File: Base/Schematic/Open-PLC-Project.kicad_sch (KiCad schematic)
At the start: 0 parts

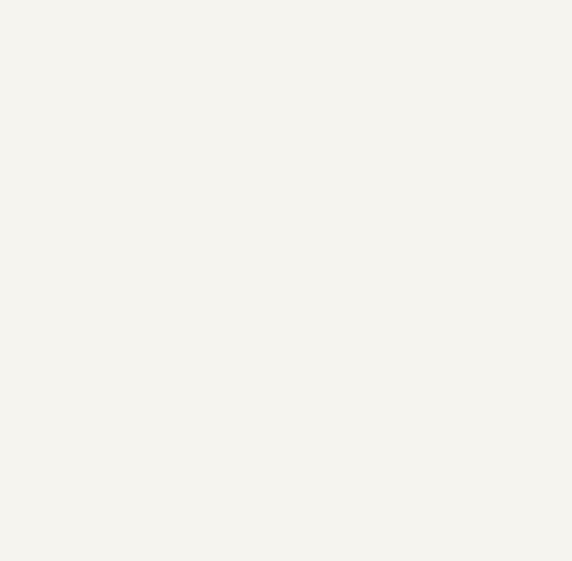
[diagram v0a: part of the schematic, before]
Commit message: [Base 회로 업데이트] - 전원 회로 추가
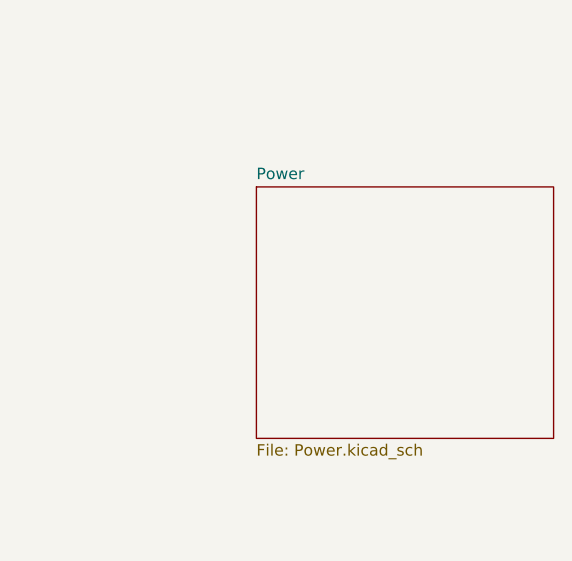
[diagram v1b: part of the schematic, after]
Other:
- added sheet Power (Power.kicad_sch)
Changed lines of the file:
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@@
+		)
+	)
+	(sheet
+		(at 223.52 127)
+		(size 33.02 27.94)
+		(fields_autoplaced yes)
+		(stroke
+			(width 0.1524)
+			(type solid)
+		)
+		(fill
+			(color 0 0 0 0.0000)
+		)
+		(property "Sheetname" "Power"
+			(at 223.52 126.2884 0)
+			(effects
+				(font
+					(size 1.27 1.27)
+				)
+				(justify left bottom)
+			)
+		)
+		(property "Sheetfile" "Power.kicad_sch"
+			(at 223.52 155.5246 0)
+			(effects
+				(font
+					(size 1.27 1.27)
+				)
+				(justify left top)
+			)
+		)
+		(instances
+			(project "Open-PLC-Project"
+				(path "/0d177ca6-e392-45a0-9514-d370436392ef"
+					(page "3")
+				)
+			)
 		)
 	)

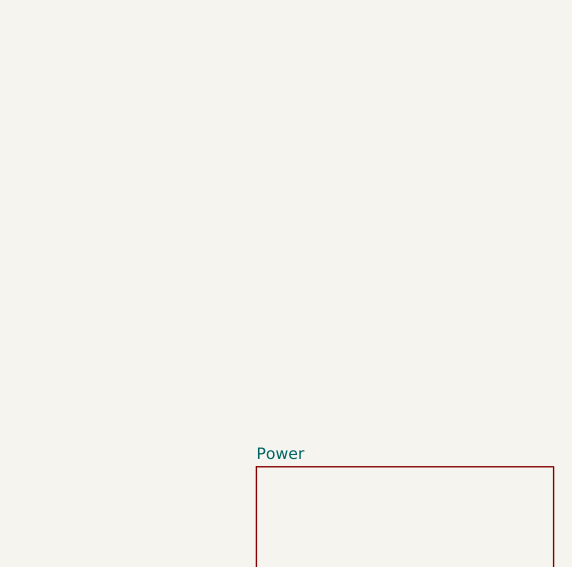
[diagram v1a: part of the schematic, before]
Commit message: [BOM 문서 테스트] - Libreoffice로 BOM 문서 출력 테스트 - 회로도에 CAN transceiver 추가
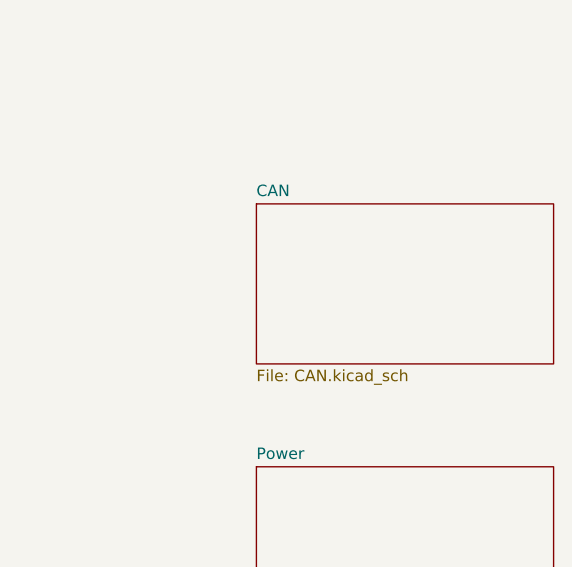
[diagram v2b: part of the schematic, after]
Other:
- added sheet CAN (CAN.kicad_sch)
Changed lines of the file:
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@@
+		)
+	)
+	(sheet
+		(at 223.52 97.79)
+		(size 33.02 17.78)
+		(fields_autoplaced yes)
+		(stroke
+			(width 0.1524)
+			(type solid)
+		)
+		(fill
+			(color 0 0 0 0.0000)
+		)
+		(property "Sheetname" "CAN"
+			(at 223.52 97.0784 0)
+			(effects
+				(font
+					(size 1.27 1.27)
+				)
+				(justify left bottom)
+			)
+		)
+		(property "Sheetfile" "CAN.kicad_sch"
+			(at 223.52 116.1546 0)
+			(effects
+				(font
+					(size 1.27 1.27)
+				)
+				(justify left top)
+			)
+		)
+		(instances
+			(project "Open-PLC-Project"
+				(path "/0d177ca6-e392-45a0-9514-d370436392ef"
+					(page "4")
+				)
+			)
 		)
 	)

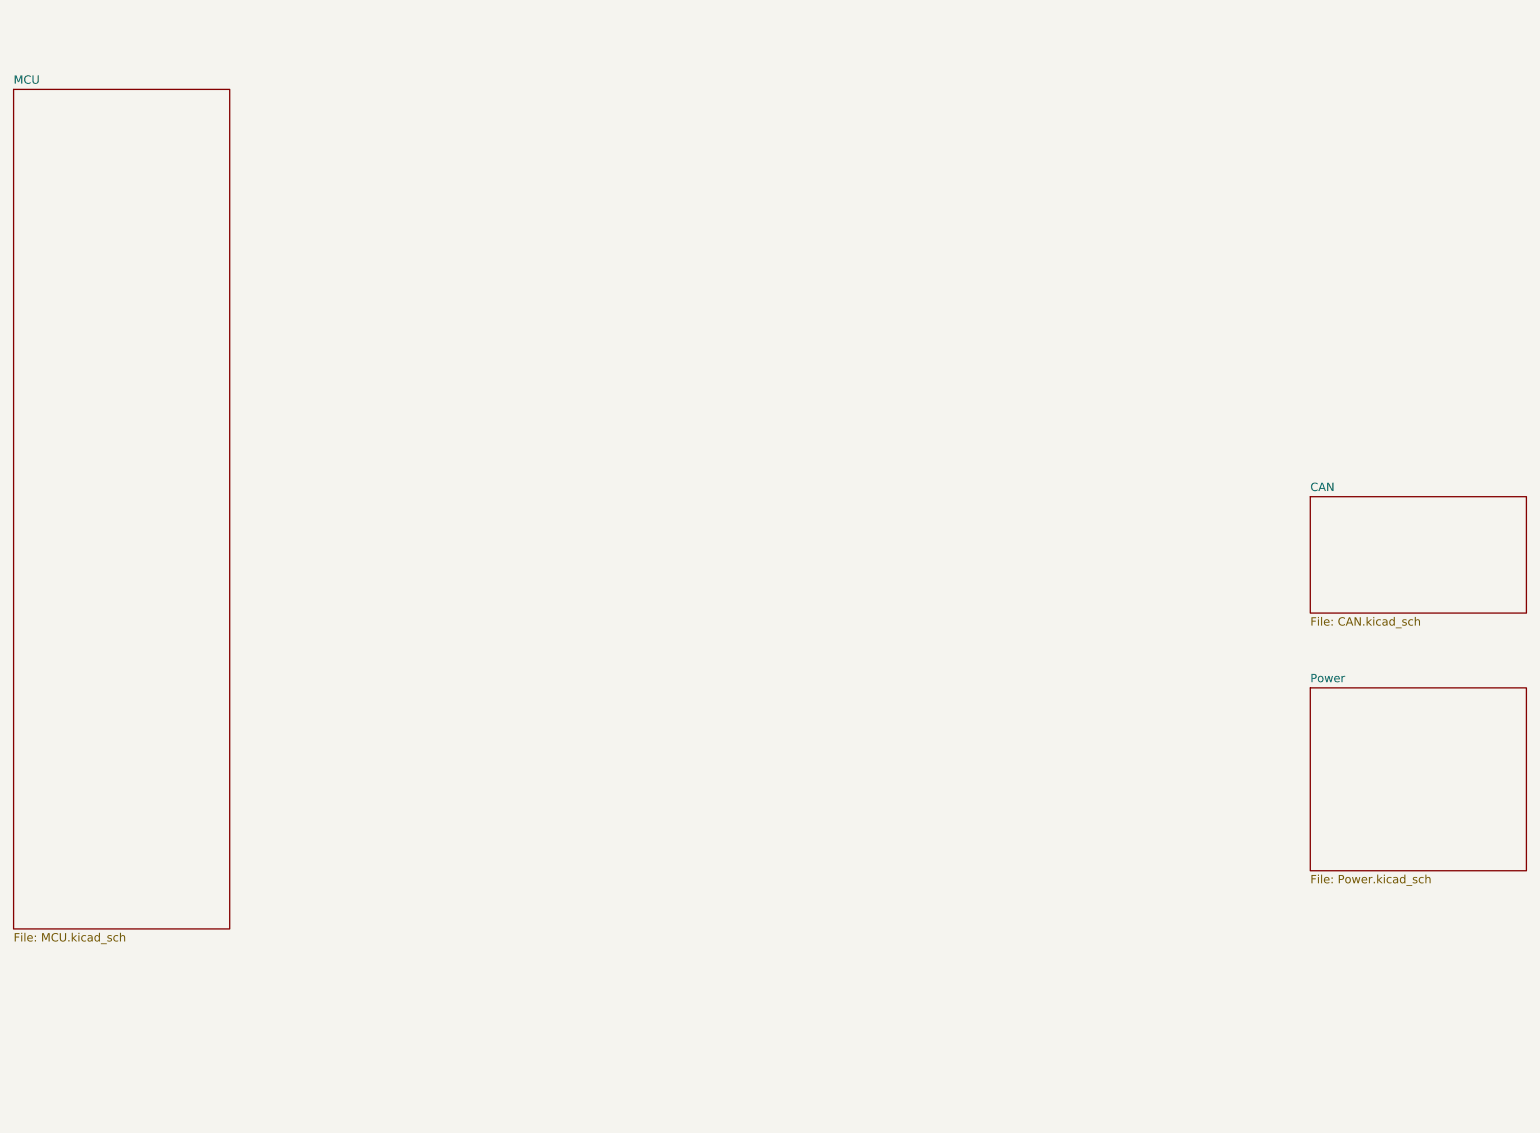
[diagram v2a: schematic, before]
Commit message: [Base 회로도 업데이트] - RS485 회로 추가
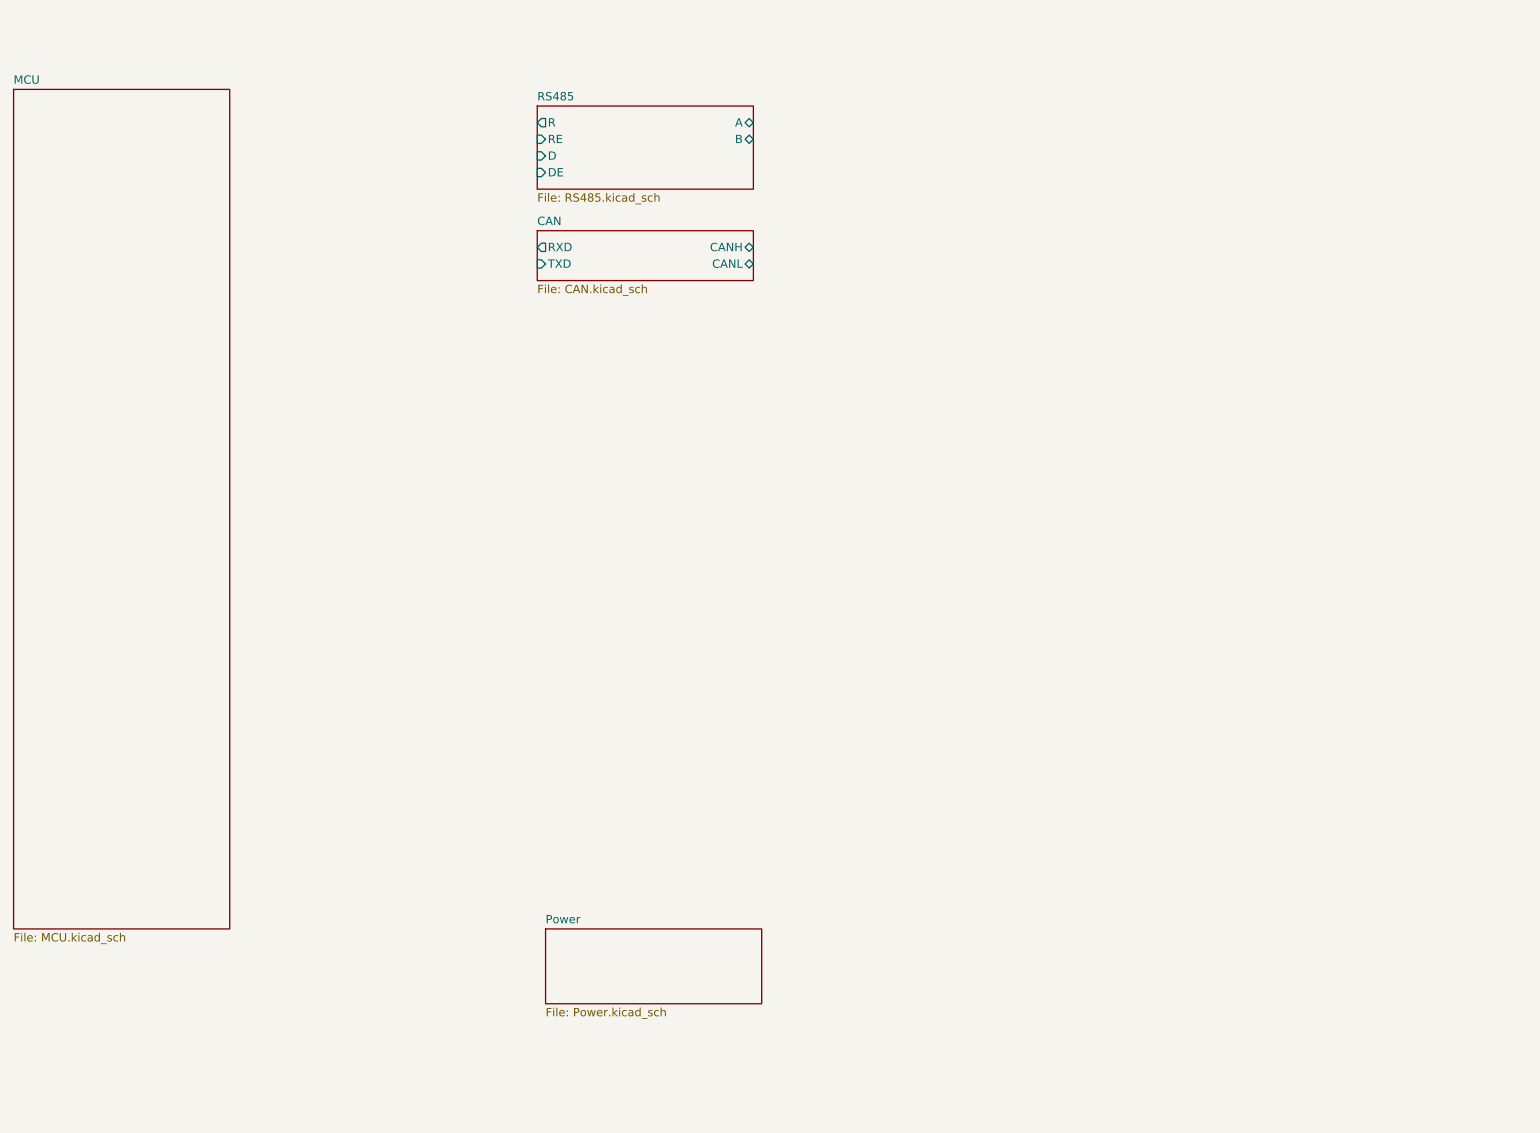
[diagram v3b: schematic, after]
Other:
- added sheet RS485 (RS485.kicad_sch)
- sheet CAN ports: added CANH, CANL, RXD, TXD; removed none
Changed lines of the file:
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@@
 	)
 	(sheet
-		(at 223.52 127)
-		(size 33.02 27.94)
+		(at 106.68 163.83)
+		(size 33.02 11.43)
 		(fields_autoplaced yes)
 		(stroke
@@
 		)
 		(property "Sheetname" "Power"
-			(at 223.52 126.2884 0)
+			(at 106.68 163.1184 0)
 			(effects
 				(font
@@
 		)
 		(property "Sheetfile" "Power.kicad_sch"
-			(at 223.52 155.5246 0)
+			(at 106.68 175.8446 0)
 			(effects
 				(font
@@
 	)
 	(sheet
-		(at 223.52 97.79)
-		(size 33.02 17.78)
+		(at 105.41 38.1)
+		(size 33.02 12.7)
+		(fields_autoplaced yes)
+		(stroke
+			(width 0.1524)
+			(type solid)
+		)
+		(fill
+			(color 0 0 0 0.0000)
+		)
+		(property "Sheetname" "RS485"
+			(at 105.41 37.3884 0)
+			(effects
+				(font
+					(size 1.27 1.27)
+				)
+				(justify left bottom)
+			)
+		)
+		(property "Sheetfile" "RS485.kicad_sch"
+			(at 105.41 51.3846 0)
+			(effects
+				(font
+					(size 1.27 1.27)
+				)
+				(justify left top)
+			)
+		)
+		(pin "RE" input
+			(at 105.41 43.18 180)
+			(effects
+				(font
+					(size 1.27 1.27)
+				)
+				(justify left)
+			)
+		)
+		(pin "D" input
+			(at 105.41 45.72 180)
+			(effects
+				(font
+					(size 1.27 1.27)
+				)
+				(justify left)
+			)
+		)
+		(pin "DE" input
+			(at 105.41 48.26 180)
+			(effects
+				(font
+					(size 1.27 1.27)
+				)
+				(justify left)
+			)
+		)
+		(pin "R" output
+			(at 105.41 40.64 180)
+			(effects
+				(font
+					(size 1.27 1.27)
+				)
+				(justify left)
+			)
+		)
+		(pin "A" bidirectional
+			(at 138.43 40.64 0)
+			(effects
+				(font
+					(size 1.27 1.27)
+				)
+				(justify right)
+			)
+		)
+		(pin "B" bidirectional
+			(at 138.43 43.18 0)
+			(effects
+				(font
+					(size 1.27 1.27)
+				)
+				(justify right)
+			)
+		)
+		(instances
+			(project "Open-PLC-Project"
+				(path "/0d177ca6-e392-45a0-9514-d370436392ef"
+					(page "5")
+				)
+			)
+		)
+	)
+	(sheet
+		(at 105.41 57.15)
+		(size 33.02 7.62)
 		(fields_autoplaced yes)
 		(stroke
@@
 		)
 		(property "Sheetname" "CAN"
-			(at 223.52 97.0784 0)
+			(at 105.41 56.4384 0)
 			(effects
 				(font
@@
 		)
 		(property "Sheetfile" "CAN.kicad_sch"
-			(at 223.52 116.1546 0)
+			(at 105.41 65.3546 0)
 			(effects
 				(font
@@
 			)
 		)
+		(pin "RXD" output
+			(at 105.41 59.69 180)
+			(effects
+				(font
+					(size 1.27 1.27)
+				)
+				(justify left)
+			)
+		)
+		(pin "TXD" input
+			(at 105.41 62.23 180)
+			(effects
+				(font
+					(size 1.27 1.27)
+				)
+				(justify left)
+			)
+		)
+		(pin "CANH" bidirectional
+			(at 138.43 59.69 0)
+			(effects
+				(font
+					(size 1.27 1.27)
+				)
+				(justify right)
+			)
+		)
+		(pin "CANL" bidirectional
+			(at 138.43 62.23 0)
+			(effects
+				(font
+					(size 1.27 1.27)
+				)
+				(justify right)
+			)
+		)

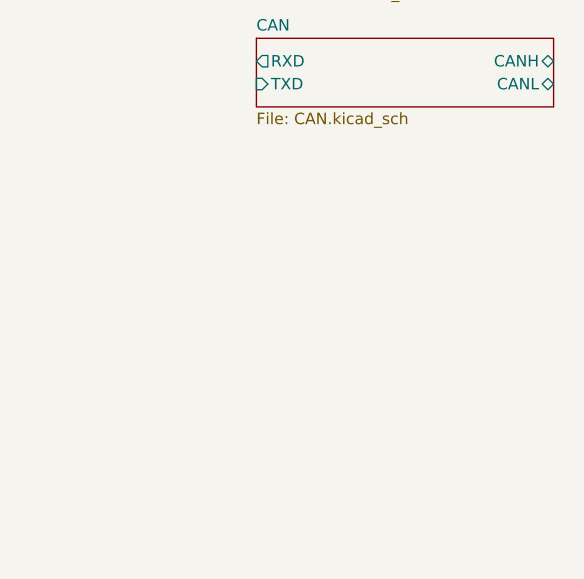
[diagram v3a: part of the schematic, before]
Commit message: [Base 회로도 업데이트] - DOUT 회로 추가
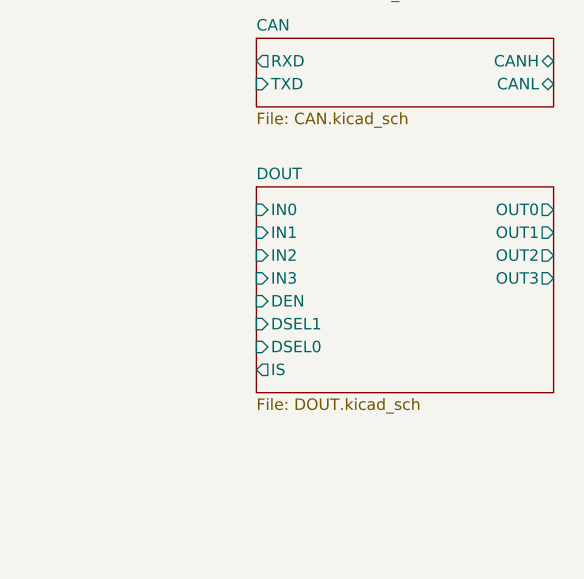
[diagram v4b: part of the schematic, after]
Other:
- added sheet DOUT (DOUT.kicad_sch)
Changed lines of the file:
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@@
+	)
+	(sheet
+		(at 105.41 73.66)
+		(size 33.02 22.86)
+		(fields_autoplaced yes)
+		(stroke
+			(width 0.1524)
+			(type solid)
+		)
+		(fill
+			(color 0 0 0 0.0000)
+		)
+		(property "Sheetname" "DOUT"
+			(at 105.41 72.9484 0)
+			(effects
+				(font
+					(size 1.27 1.27)
+				)
+				(justify left bottom)
+			)
+		)
+		(property "Sheetfile" "DOUT.kicad_sch"
+			(at 105.41 97.1046 0)
+			(effects
+				(font
+					(size 1.27 1.27)
+				)
+				(justify left top)
+			)
+		)
+		(pin "OUT2" output
+			(at 138.43 81.28 0)
+			(effects
+				(font
+					(size 1.27 1.27)
+				)
+				(justify right)
+			)
+		)
+		(pin "OUT0" output
+			(at 138.43 76.2 0)
+			(effects
+				(font
+					(size 1.27 1.27)
+				)
+				(justify right)
+			)
+		)
+		(pin "OUT1" output
+			(at 138.43 78.74 0)
+			(effects
+				(font
+					(size 1.27 1.27)
+				)
+				(justify right)
+			)
+		)
+		(pin "OUT3" output
+			(at 138.43 83.82 0)
+			(effects
+				(font
+					(size 1.27 1.27)
+				)
+				(justify right)
+			)
+		)
+		(pin "IS" output
+			(at 105.41 93.98 180)
+			(effects
+				(font
+					(size 1.27 1.27)
+				)
+				(justify left)
+			)
+		)
+		(pin "IN0" input
+			(at 105.41 76.2 180)
+			(effects
+				(font
+					(size 1.27 1.27)
+				)
+				(justify left)
+			)
+		)
+		(pin "IN2" input
+			(at 105.41 81.28 180)
+			(effects
+				(font
+					(size 1.27 1.27)
+				)
+				(justify left)
+			)
+		)
+		(pin "IN1" input
+			(at 105.41 78.74 180)
+			(effects
+				(font
+					(size 1.27 1.27)
+				)
+				(justify left)
+			)
+		)
+		(pin "IN3" input
+			(at 105.41 83.82 180)
+			(effects
+				(font
+					(size 1.27 1.27)
+				)
+				(justify left)
+			)
+		)
+		(pin "DEN" input
+			(at 105.41 86.36 180)
+			(effects
+				(font
+					(size 1.27 1.27)
+				)
+				(justify left)
+			)
+		)
+		(pin "DSEL1" input
+			(at 105.41 88.9 180)
+			(effects
+				(font
+					(size 1.27 1.27)
+				)
+				(justify left)
+			)
+		)
+		(pin "DSEL0" input
+			(at 105.41 91.44 180)
+			(effects
+				(font
+					(size 1.27 1.27)
+				)
+				(justify left)
+			)
+		)
+		(instances
+			(project "Open-PLC-Project"
+				(path "/0d177ca6-e392-45a0-9514-d370436392ef"
+					(page "6")
+				)
+			)
+		)
 	)
 	(sheet

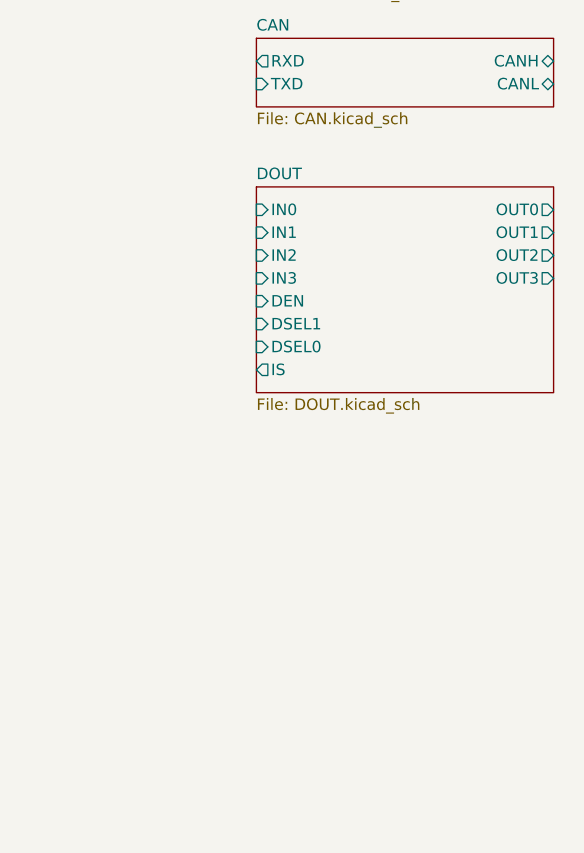
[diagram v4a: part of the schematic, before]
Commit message: [Base 회로도 업데이트] - DOUT 출력을 4개에서 8개로 늘림
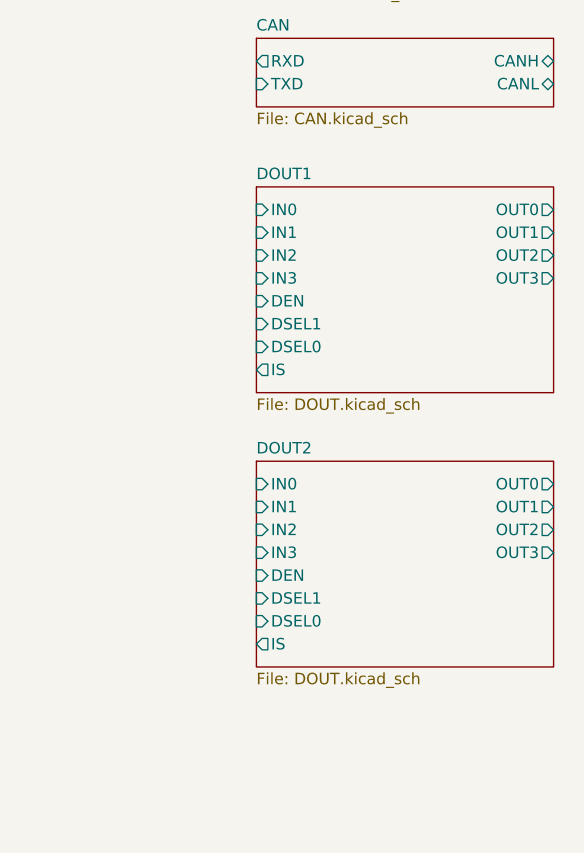
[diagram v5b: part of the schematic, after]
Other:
- sheet DOUT renamed DOUT1
- added sheet DOUT2 (DOUT.kicad_sch)
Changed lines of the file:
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@@
+	)
+	(sheet
+		(at 105.41 104.14)
+		(size 33.02 22.86)
+		(fields_autoplaced yes)
+		(stroke
+			(width 0.1524)
+			(type solid)
+		)
+		(fill
+			(color 0 0 0 0.0000)
+		)
+		(property "Sheetname" "DOUT2"
+			(at 105.41 103.4284 0)
+			(effects
+				(font
+					(size 1.27 1.27)
+				)
+				(justify left bottom)
+			)
+		)
+		(property "Sheetfile" "DOUT.kicad_sch"
+			(at 105.41 127.5846 0)
+			(effects
+				(font
+					(size 1.27 1.27)
+				)
+				(justify left top)
+			)
+		)
+		(pin "OUT2" output
+			(at 138.43 111.76 0)
+			(effects
+				(font
+					(size 1.27 1.27)
+				)
+				(justify right)
+			)
+		)
+		(pin "OUT0" output
+			(at 138.43 106.68 0)
+			(effects
+				(font
+					(size 1.27 1.27)
+				)
+				(justify right)
+			)
+		)
+		(pin "OUT1" output
+			(at 138.43 109.22 0)
+			(effects
+				(font
+					(size 1.27 1.27)
+				)
+				(justify right)
+			)
+		)
+		(pin "OUT3" output
+			(at 138.43 114.3 0)
+			(effects
+				(font
+					(size 1.27 1.27)
+				)
+				(justify right)
+			)
+		)
+		(pin "IS" output
+			(at 105.41 124.46 180)
+			(effects
+				(font
+					(size 1.27 1.27)
+				)
+				(justify left)
+			)
+		)
+		(pin "IN0" input
+			(at 105.41 106.68 180)
+			(effects
+				(font
+					(size 1.27 1.27)
+				)
+				(justify left)
+			)
+		)
+		(pin "IN2" input
+			(at 105.41 111.76 180)
+			(effects
+				(font
+					(size 1.27 1.27)
+				)
+				(justify left)
+			)
+		)
+		(pin "IN1" input
+			(at 105.41 109.22 180)
+			(effects
+				(font
+					(size 1.27 1.27)
+				)
+				(justify left)
+			)
+		)
+		(pin "IN3" input
+			(at 105.41 114.3 180)
+			(effects
+				(font
+					(size 1.27 1.27)
+				)
+				(justify left)
+			)
+		)
+		(pin "DEN" input
+			(at 105.41 116.84 180)
+			(effects
+				(font
+					(size 1.27 1.27)
+				)
+				(justify left)
+			)
+		)
+		(pin "DSEL1" input
+			(at 105.41 119.38 180)
+			(effects
+				(font
+					(size 1.27 1.27)
+				)
+				(justify left)
+			)
+		)
+		(pin "DSEL0" input
+			(at 105.41 121.92 180)
+			(effects
+				(font
+					(size 1.27 1.27)
+				)
+				(justify left)
+			)
+		)
+		(instances
+			(project "Open-PLC-Project"
+				(path "/0d177ca6-e392-45a0-9514-d370436392ef"
+					(page "7")
+				)
+			)
+		)
 	)
 	(sheet
@@
 			(color 0 0 0 0.0000)
 		)
-		(property "Sheetname" "DOUT"
+		(property "Sheetname" "DOUT1"
 			(at 105.41 72.9484 0)
 			(effects
